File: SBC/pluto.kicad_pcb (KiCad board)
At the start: 4 copper layers, 114.3 x 120.9 mm, 60 parts, among them J1 VCC1, J10 GND3, J11 Expansion Bus, J2 GND1, J3 VCC2, J4 POWER, J5 GND2, J6 RS232a, J7 RS232b, J8 JTAG, J9 VCC3, P1 IDE0, SW1 RESET, U1 WD65C02PLCC44, U19 74LS574, U2 28C256, U20 74LS574, U21 74HC245, U22 MAX238, U23 SC28L92PLCC44, U3 AS6C62256A, U4 DS1511Y+, U5 TL7705B, U7 ispMACH4A5, U8 74HC74, X1 8 MHz, X2 3.6864MHz

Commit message: Preparation for Pluto v3.0
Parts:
- removed C21, C22: 0.1uF, Capacitors_ThroughHole:C_Disc_D4.7mm_W2.5mm_P5.00mm
- removed J8: JTAG, Connectors_IDC:IDC-Header_2x05_Pitch2.54mm_Straight
- removed MK2, MK5: Mounting_Hole, Mounting_Holes:MountingHole_3.2mm_M3_Pad
- removed R7: 1K, Resistors_ThroughHole:R_Axial_DIN0411_L9.9mm_D3.6mm_P12.70mm_Horizontal
- removed RN2: 3.3 kOhm, Resistors_THT:R_Array_SIP8
- removed U19, U20: 74LS574, Housings_DIP:DIP-20_W7.62mm_Socket
- removed U21: 74HC245, Housings_DIP:DIP-20_W7.62mm_Socket
- added C7: 0.1uF, Capacitor_THT:C_Disc_D4.7mm_W2.5mm_P5.00mm, F.Cu at (68.0, 97.2)
- added C8: 0.1uF, Capacitor_THT:C_Disc_D4.7mm_W2.5mm_P5.00mm, F.Cu at (86.3, 103.5)
- added C9: 0.1uF, Capacitor_THT:C_Disc_D4.7mm_W2.5mm_P5.00mm, F.Cu at (100.3, 82.5)
- added D2: DIRQ1, Diode_THT:D_T-1_P5.08mm_Horizontal, F.Cu at (86.4, 97.2)
- added D4: DIRQ2, Diode_THT:D_T-1_P5.08mm_Horizontal, F.Cu at (73.0, 103.5)
- added J12: VIA2PB, Connector_IDC:IDC-Header_2x07_P2.54mm_Vertical, F.Cu at (73.0, 136.5)
- added Q1: DS1813, Package_TO_SOT_THT:TO-92L_Inline, F.Cu at (125.7, 68.6)
- added SW2: PANIC, Button_Switch_THT:SW_PUSH_6mm_H4.3mm, F.Cu at (121.9, 62.9)
- added U6: PlutoDecoder, Package_DIP:DIP-24_W7.62mm_Socket, F.Cu at (95.2, 93.3)
- added U9: WD65C22PLCC44, Package_LCC:PLCC-44_THT-Socket, F.Cu at (71.8, 116.2)
- C1, C2, C20, C3, C5, C6: footprint Capacitors_ThroughHole:C_Disc_D4.7mm_W2.5mm_P5.00mm -> Capacitor_THT:C_Disc_D4.7mm_W2.5mm_P5.00mm
- C15, C16, C17, C18, C19, C4: footprint Capacitors_ThroughHole:CP_Radial_Tantal_D4.5mm_P2.50mm -> Capacitor_THT:CP_Radial_Tantal_D4.5mm_P2.50mm
- F1: footprint Fuse_Holders_and_Fuses:Fuseholder5x20_horiz_open_Schurter_0031_8201 -> Fuse:Fuseholder_Cylinder-5x20mm_Schurter_0031_8201_Horizontal_Open
- J1, J10, J2, J3, J5, J9: footprint Pin_Headers:Pin_Header_Straight_1x01_Pitch2.54mm -> Connector_PinHeader_2.54mm:PinHeader_1x01_P2.54mm_Vertical
- J11, P1: footprint Connectors_IDC:IDC-Header_2x20_Pitch2.54mm_Straight -> Connector_IDC:IDC-Header_2x20_P2.54mm_Vertical
- J4: footprint Connectors_Molex:Molex_NanoFit_1x04x2.50mm_Angled -> Connector_Molex:Molex_Nano-Fit_105313-xx04_1x04_P2.50mm_Horizontal
- J6, J7: footprint Connectors_IDC:IDC-Header_2x05_Pitch2.54mm_Straight -> Connector_IDC:IDC-Header_2x05_P2.54mm_Vertical
- MK1, MK3, MK4, MK6: footprint Mounting_Holes:MountingHole_3.2mm_M3_Pad -> MountingHole:MountingHole_3.2mm_M3_Pad
- R1, R6, R8: footprint Resistors_ThroughHole:R_Axial_DIN0411_L9.9mm_D3.6mm_P12.70mm_Horizontal -> Resistor_THT:R_Axial_DIN0411_L9.9mm_D3.6mm_P7.62mm_Vertical
- R2, R3, R4: footprint Resistors_ThroughHole:R_Axial_DIN0411_L9.9mm_D3.6mm_P7.62mm_Vertical -> Resistor_THT:R_Axial_DIN0411_L9.9mm_D3.6mm_P7.62mm_Vertical
- RN1: value 3.3 kOhm -> 3.3k; footprint Resistors_THT:R_Array_SIP8 -> Resistor_THT:R_Array_SIP9
- SW1: footprint Buttons_Switches_ThroughHole:SW_PUSH_6mm_h4.3mm -> Button_Switch_THT:SW_PUSH_6mm_H4.3mm
- U1, U23: footprint Housings_LCC:PLCC-44_THT-Socket -> Package_LCC:PLCC-44_THT-Socket
- U2: value 28C256 -> AT28HC256EPLCC32; footprint Housings_DIP:DIP-28_W15.24mm_Socket -> Grotto:PLCC-32_THT-Socket
- U22: footprint Housings_DIP:DIP-24_W7.62mm_Socket -> Package_DIP:DIP-24_W7.62mm_Socket
- U3: footprint Housings_DIP:DIP-28_W15.24mm_Socket -> Package_DIP:DIP-28_W7.62mm_Socket
- U4: footprint Housings_DIP:DIP-28_W15.24mm_Socket -> Package_DIP:DIP-28_W15.24mm_Socket
- U5: footprint Housings_DIP:DIP-8_W7.62mm_Socket -> Package_DIP:DIP-8_W7.62mm_Socket
- U7: value ispMACH4A5 -> WD65C22PLCC44; footprint Housings_LCC:PLCC-44_THT-Socket -> Package_LCC:PLCC-44_THT-Socket
- U8: footprint Housings_DIP:DIP-14_W7.62mm_Socket -> Package_DIP:DIP-14_W7.62mm_Socket
- X1, X2: footprint Oscillators:Oscillator_DIP-8 -> Oscillator:Oscillator_DIP-8
- moved J2 94.1 mm to (158.2, 59.1), turned to 90 degrees
- moved C2 86.4 mm to (150.5, 72.4), turned to 0 degrees
- moved J1 85.4 mm to (158.2, 62.9), turned to 90 degrees
- moved R3 78.1 mm to (139.7, 59.7), turned to 180 degrees
- moved R2 76.3 mm to (154.3, 47.0), turned to 270 degrees
- moved C4 72.6 mm to (132.1, 55.9), turned to 90 degrees
- moved R4 68.7 mm to (137.8, 54.0), turned to 90 degrees
- moved U3 62.3 mm to (149.2, 75.6), turned to 0 degrees
- moved U2 60.8 mm to (136.5, 90.8), turned to 0 degrees
- moved J11 60.0 mm to (104.8, 136.1), turned to 90 degrees
- moved C3 53.9 mm to (139.7, 78.1), turned to 180 degrees
- moved U8 51.3 mm to (95.2, 62.2), turned to 0 degrees
- moved RN1 46.7 mm to (115.6, 99.1), turned to 180 degrees
- moved U1 39.1 mm to (108.0, 123.8), turned to 180 degrees
- moved J3 36.6 mm to (130.7, 49.4), turned to 270 degrees
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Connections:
- net /16bit IDE interface/~IDE:DASP renamed /16bit IDE interface/~IDE-DASP
- net /16bit IDE interface/~IDE:DMACK renamed /16bit IDE interface/~IDE-DMACK
- J11 pad 24: /Address decoding and support section/R/~W -> /16bit IDE interface/R-~W
- J11 pad 34: /Address decoding and support section/~7FCX -> /Address decoding and support section/~IO
- J11 pad 36: /Address decoding and support section/~7FAX -> Net-(J11-Pad36)
- J11 pad 38: /Address decoding and support section/CLK -> /16bit IDE interface/CLK
- J11 pad 9: /Address decoding and support section/A3 -> /16bit IDE interface/A3
- P1 pad 1: /16bit IDE interface/~RES -> /16bit IDE interface/~IDE-RES
- P1 pad 23: /16bit IDE interface/DIOW -> /16bit IDE interface/~DIOW
- P1 pad 25: /16bit IDE interface/DIOR -> /16bit IDE interface/~DIOR
- P1 pad 33: /16bit IDE interface/A1 -> /16bit IDE interface/IDE-A1
- P1 pad 35: /16bit IDE interface/A0 -> /16bit IDE interface/IDE-A0
- P1 pad 36: /16bit IDE interface/A2 -> /16bit IDE interface/IDE-A2
- P1 pad 37: /16bit IDE interface/IDE_CS0 -> /16bit IDE interface/~IDE-CS0
- P1 pad 38: /16bit IDE interface/~IDE:CS1 -> /16bit IDE interface/~IDE-CS1
- R2 pad 1: Net-(R2-Pad1) -> VCC
- R2 pad 2: VCC -> Net-(R2-Pad2)
- RN1 pad 2: Net-(RN1-Pad2) -> /16bit IDE interface/~RES
- RN1 pad 4: /Address decoding and support section/TDO -> /Address decoding and support section/~SO
- RN1 pad 5: /Address decoding and support section/TDI -> /Address decoding and support section/RDY
- RN1 pad 6: /Address decoding and support section/TMS -> /Address decoding and support section/~PWR
- RN1 pad 7: /Address decoding and support section/TCK -> /Address decoding and support section/BE
- RN1 pad 8: /Address decoding and support section/~SO -> /Address decoding and support section/~NMI
- SW1 pad 2: Net-(R2-Pad1) -> Net-(R2-Pad2)
- U1 pad 14: /Address decoding and support section/A3 -> /16bit IDE interface/A3
- U1 pad 38: /Address decoding and support section/R/~W -> /16bit IDE interface/R-~W
- U1 pad 41: /Address decoding and support section/CLK -> /16bit IDE interface/CLK
- U2 pad 1: /Address decoding and support section/A14 -> Net-(U2-Pad1)
- U2 pad 10: /16bit IDE interface/A0 -> /16bit IDE interface/A1
- U2 pad 11: /16bit IDE interface/D0 -> /16bit IDE interface/A0
- U2 pad 12: /16bit IDE interface/D1 -> Net-(U2-Pad12)
- U2 pad 13: /16bit IDE interface/D2 -> /16bit IDE interface/D0
- U2 pad 14: GND -> /16bit IDE interface/D1
- U2 pad 15: /16bit IDE interface/D3 -> /16bit IDE interface/D2
- U2 pad 16: /16bit IDE interface/D4 -> GND
- U2 pad 17: /16bit IDE interface/D5 -> Net-(U2-Pad17)
- U2 pad 18: /16bit IDE interface/D6 -> /16bit IDE interface/D3
- U2 pad 19: /16bit IDE interface/D7 -> /16bit IDE interface/D4
- U2 pad 2: /Address decoding and support section/A12 -> /Address decoding and support section/A14
- U2 pad 20: /Address decoding and support section/~ROMSEL -> /16bit IDE interface/D5
- U2 pad 21: /Address decoding and support section/A10 -> /16bit IDE interface/D6
- U2 pad 22: /Address decoding and support section/~MRD -> /16bit IDE interface/D7
- U2 pad 23: /Address decoding and support section/A11 -> /Address decoding and support section/~ROMSEL
- U2 pad 24: /Address decoding and support section/A9 -> /Address decoding and support section/A10
- U2 pad 25: /Address decoding and support section/A8 -> /Address decoding and support section/~MRD
- U2 pad 26: /Address decoding and support section/A13 -> Net-(U2-Pad26)
- U2 pad 27: VCC -> /Address decoding and support section/A11
- U2 pad 28: VCC -> /Address decoding and support section/A9
- U2 pad 3: /Address decoding and support section/A7 -> /Address decoding and support section/A12
- U2 pad 4: /Address decoding and support section/A6 -> /Address decoding and support section/A7
- U2 pad 5: /Address decoding and support section/A5 -> /Address decoding and support section/A6
- U2 pad 6: /CPU, ROM and RAM/A4 -> /Address decoding and support section/A5
- U2 pad 7: /Address decoding and support section/A3 -> /CPU, ROM and RAM/A4
- U2 pad 8: /16bit IDE interface/A2 -> /16bit IDE interface/A3
- U2 pad 9: /16bit IDE interface/A1 -> /16bit IDE interface/A2
- U23 pad 39: /Address decoding and support section/~7FEX -> /Address decoding and support section/~DUART
- U23 pad 7: /Address decoding and support section/A3 -> /16bit IDE interface/A3
- U3 pad 7: /Address decoding and support section/A3 -> /16bit IDE interface/A3
- U4 pad 20: /Address decoding and support section/~7F8X -> /Address decoding and support section/~RTC
- U4 pad 7: /Address decoding and support section/A3 -> /16bit IDE interface/A3
- U5 pad 2: Net-(R2-Pad1) -> Net-(R2-Pad2)
- U7 pad 10: /Address decoding and support section/TDI -> /16bit IDE interface/IDE-D8
- U7 pad 11: /Address decoding and support section/CLK -> Net-(U7-Pad11)
- U7 pad 12: GND -> /16bit IDE interface/IDE-D9
- U7 pad 13: /Address decoding and support section/TCK -> /16bit IDE interface/IDE-D10
- U7 pad 14: /Address decoding and support section/A13 -> /16bit IDE interface/IDE-D11
- U7 pad 15: /Address decoding and support section/~RAMSEL -> /16bit IDE interface/IDE-D12
- U7 pad 16: /Address decoding and support section/A12 -> /16bit IDE interface/IDE-D13
- U7 pad 17: /16bit IDE interface/FROM_CLK -> /16bit IDE interface/IDE-D14
- U7 pad 18: /Address decoding and support section/A11 -> /16bit IDE interface/IDE-D15
- U7 pad 19: /16bit IDE interface/IDE_CS0 -> Net-(U7-Pad19)
- U7 pad 2: /Address decoding and support section/~7FAX -> /16bit IDE interface/IDE-D0
- U7 pad 20: /16bit IDE interface/OBT_OE -> Net-(U7-Pad20)
- U7 pad 21: /Address decoding and support section/~ROMSEL -> VCC
- U7 pad 22: VCC -> Net-(U7-Pad22)
- U7 pad 23: GND -> Net-(D2-Pad1)
- U7 pad 24: /16bit IDE interface/FROM_OE -> /16bit IDE interface/R-~W
- U7 pad 25: /16bit IDE interface/DIOW -> /16bit IDE interface/~VIA1SEL
- U7 pad 26: /16bit IDE interface/TO_OE -> VCC
- U7 pad 27: /Address decoding and support section/A10 -> /16bit IDE interface/CLK
- U7 pad 28: /16bit IDE interface/OBT_DIR -> /16bit IDE interface/D7
- U7 pad 29: /Address decoding and support section/A9 -> /16bit IDE interface/D6
- U7 pad 3: /Address decoding and support section/~7FEX -> /16bit IDE interface/IDE-D1
- U7 pad 30: /16bit IDE interface/TO_CLK -> /16bit IDE interface/D5
- U7 pad 31: /Address decoding and support section/A8 -> /16bit IDE interface/D4
- U7 pad 32: /Address decoding and support section/TMS -> /16bit IDE interface/D3
- U7 pad 33: /Address decoding and support section/A15 -> Net-(U7-Pad33)
- U7 pad 34: GND -> /16bit IDE interface/D2
- U7 pad 35: /Address decoding and support section/TDO -> /16bit IDE interface/D1
- U7 pad 36: /Address decoding and support section/A7 -> /16bit IDE interface/D0
- U7 pad 37: Net-(U7-Pad37) -> /16bit IDE interface/~RES
- U7 pad 38: /Address decoding and support section/A6 -> Net-(U7-Pad38)
- U7 pad 39: /16bit IDE interface/DIOR -> /16bit IDE interface/A3
- U7 pad 4: Net-(U7-Pad4) -> /16bit IDE interface/IDE-D2
- U7 pad 40: /Address decoding and support section/A5 -> /16bit IDE interface/A2
- U7 pad 41: /Address decoding and support section/~MRD -> /16bit IDE interface/A1
- U7 pad 42: Net-(U7-Pad42) -> /16bit IDE interface/A0
- U7 pad 43: /Address decoding and support section/~MWR -> Net-(U7-Pad43)
- U7 pad 44: VCC -> Net-(U7-Pad44)
- U7 pad 5: /Address decoding and support section/A3 -> /16bit IDE interface/IDE-D3
- U7 pad 6: /Address decoding and support section/~7F8X -> /16bit IDE interface/IDE-D4
- U7 pad 7: /Address decoding and support section/R/~W -> /16bit IDE interface/IDE-D5
- U7 pad 8: /Address decoding and support section/~7FCX -> /16bit IDE interface/IDE-D6
- U7 pad 9: /Address decoding and support section/A14 -> /16bit IDE interface/IDE-D7
- U8 pad 9: /Address decoding and support section/CLK -> /16bit IDE interface/CLK
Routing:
- net /16bit IDE interface/D6: track 260.5 -> 0.00 mm
- net /16bit IDE interface/D7: track 256.1 -> 0.00 mm, vias 1 -> 0
- net /16bit IDE interface/D5: track 223.3 -> 0.00 mm, vias 1 -> 0
- net /16bit IDE interface/D4: track 217.7 -> 0.00 mm, vias 2 -> 0
- net /16bit IDE interface/~IRQ: track 211.2 -> 0.00 mm, vias 1 -> 0
- net /16bit IDE interface/D3: track 205.0 -> 0.00 mm, vias 2 -> 0
- net /16bit IDE interface/A0: track 196.0 -> 0.00 mm
- net /16bit IDE interface/D0: track 194.8 -> 0.00 mm
- net /16bit IDE interface/D2: track 191.6 -> 0.00 mm, vias 1 -> 0
- net /16bit IDE interface/A1: track 189.8 -> 0.00 mm
- net /16bit IDE interface/~RES: track 186.1 -> 0.00 mm, vias 2 -> 0
- net /Address decoding and support section/~MRD: track 185.4 -> 0.00 mm, vias 1 -> 0
- net /16bit IDE interface/A2: track 185.3 -> 0.00 mm
- net /16bit IDE interface/D1: track 181.6 -> 0.00 mm, vias 2 -> 0
- net /Address decoding and support section/~MWR: track 179.2 -> 0.00 mm
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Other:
- board text added: "Pluto V3.0 Jul 2019 © Johan Groth"
- board text removed: "Pluto V2.0 Dec 2017 © Johan Groth"

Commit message: A better layout of PCB.
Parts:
- moved J9 72.9 mm to (158.1, 48.9), turned to 90 degrees
- moved J10 68.8 mm to (147.3, 48.9), turned to 90 degrees
- moved J3 28.2 mm to (158.1, 55.9), turned to 90 degrees
- moved R3 24.2 mm to (115.6, 61.6)
- moved Q1 22.9 mm to (106.7, 81.3)
- moved J5 21.8 mm to (147.3, 55.9), turned to 90 degrees
- moved C3 21.0 mm to (160.7, 80.0), turned to 90 degrees
- moved C2 20.5 mm to (132.7, 82.5)
- moved R2 18.1 mm to (136.5, 50.2), turned to 180 degrees
- moved R4 16.9 mm to (123.8, 63.5)
- moved U5 16.8 mm to (136.5, 64.1)
- moved C4 16.5 mm to (115.6, 56.5), turned to 0 degrees
- moved SW2 16.3 mm to (132.1, 75.6), turned to 180 degrees
- moved J2 11.6 mm to (147.3, 62.9)
- moved C6 10.9 mm to (140.3, 61.6), turned to 90 degrees
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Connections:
- U6 pad 14: /16bit IDE interface/~VIA2SEL -> /Address decoding and support section/~IO
- U6 pad 15: /Address decoding and support section/~DUART -> /Address decoding and support section/~RTC
- U6 pad 16: /Address decoding and support section/~RAMSEL -> /16bit IDE interface/~VIA2SEL
- U6 pad 17: /Address decoding and support section/~MRD -> /Address decoding and support section/~DUART
- U6 pad 18: /Address decoding and support section/~IO -> /Address decoding and support section/~RAMSEL
- U6 pad 19: /16bit IDE interface/R-~W -> /Address decoding and support section/~ROMSEL
- U6 pad 20: /Address decoding and support section/~MWR -> /16bit IDE interface/~VIA1SEL
- U6 pad 21: /Address decoding and support section/~ROMSEL -> /Address decoding and support section/~MWR
- U6 pad 22: /16bit IDE interface/~VIA1SEL -> /Address decoding and support section/~MRD
- U6 pad 23: /Address decoding and support section/~RTC -> /16bit IDE interface/R-~W

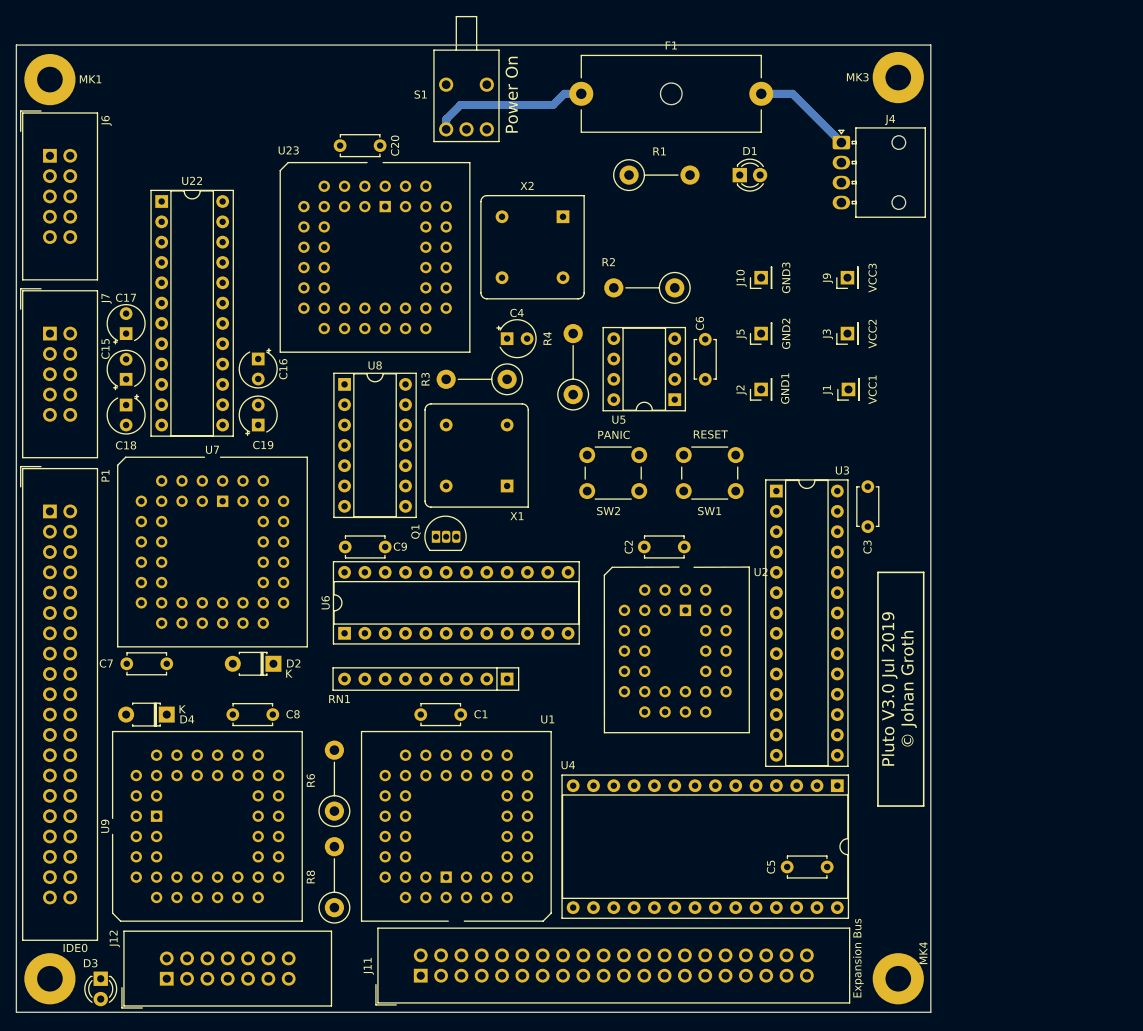
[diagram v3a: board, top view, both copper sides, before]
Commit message: Autorouting of Pluto v3.0 complete. Fixed VCC/GND and IDE-A2(!)
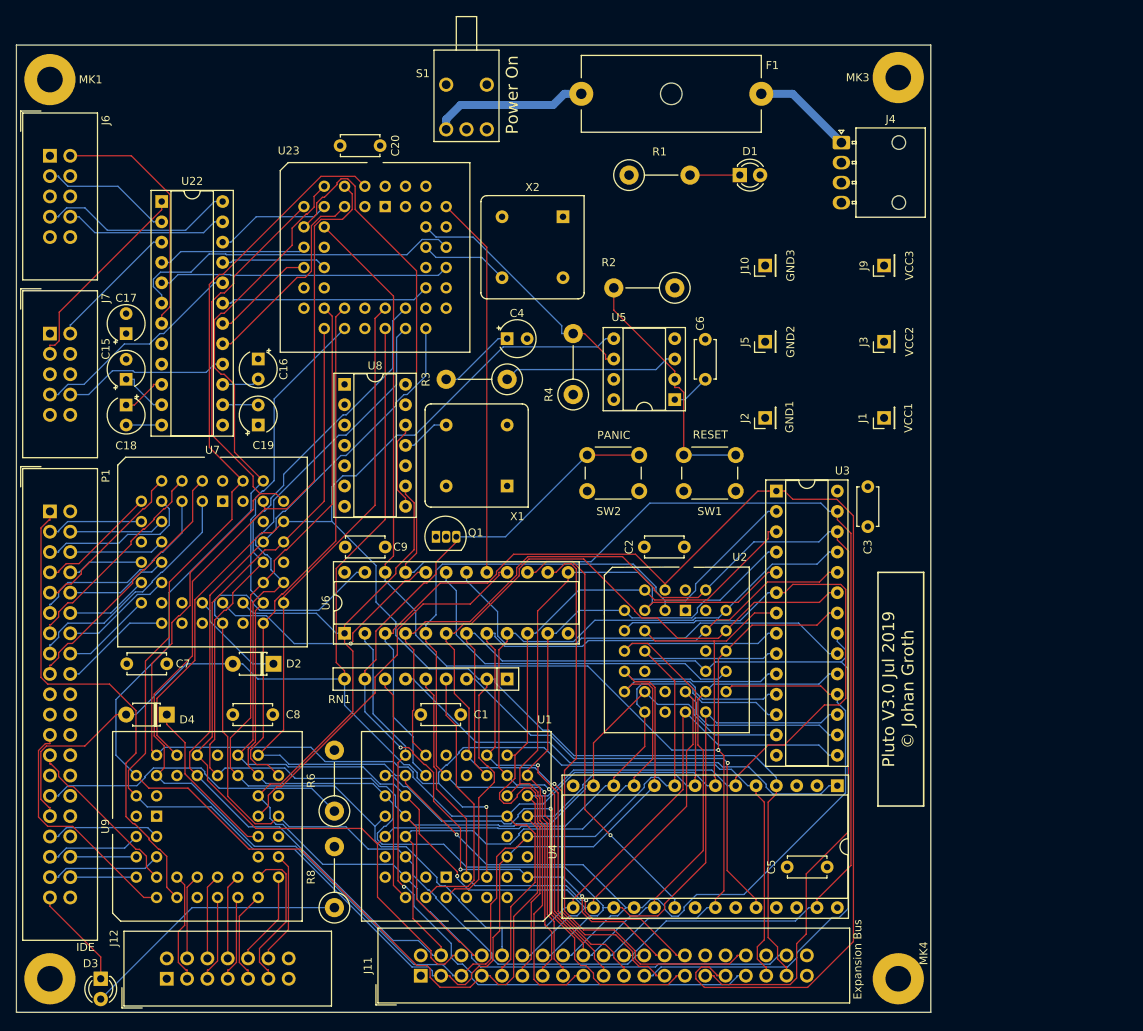
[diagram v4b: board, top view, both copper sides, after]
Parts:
- P1: value IDE0 -> IDE
- moved J1 5.69 mm to (162.7, 66.4)
- moved J9 4.82 mm to (162.7, 47.4)
- moved J3 4.68 mm to (162.7, 56.9)
- moved J2 3.59 mm to (147.8, 66.4)
- moved J10 1.61 mm to (147.8, 47.4)
- moved J5 1.14 mm to (147.8, 56.9)
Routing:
- net /16bit IDE interface/A2: track 0.00 -> 240.6 mm
- net /16bit IDE interface/A0: track 0.00 -> 226.6 mm
- net /16bit IDE interface/A3: track 0.00 -> 223.1 mm
- net /16bit IDE interface/~RES: track 0.00 -> 222.0 mm
- net /16bit IDE interface/A1: track 0.00 -> 218.1 mm
- net /16bit IDE interface/~IRQ: track 0.00 -> 203.6 mm, vias 0 -> 1
- net /Address decoding and support section/~MWR: track 0.00 -> 198.9 mm
- net /16bit IDE interface/D0: track 0.00 -> 196.8 mm
- net /16bit IDE interface/D6: track 0.00 -> 190.3 mm, vias 0 -> 1
- net /16bit IDE interface/D4: track 0.00 -> 186.0 mm, vias 0 -> 1
- net /16bit IDE interface/D7: track 0.00 -> 182.1 mm, vias 0 -> 1
- net /16bit IDE interface/D5: track 0.00 -> 181.3 mm
- net /16bit IDE interface/D2: track 0.00 -> 179.5 mm
- net /16bit IDE interface/D1: track 0.00 -> 176.9 mm
- net /16bit IDE interface/D3: track 0.00 -> 173.7 mm
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
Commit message: Converting to SMD of almost all components.
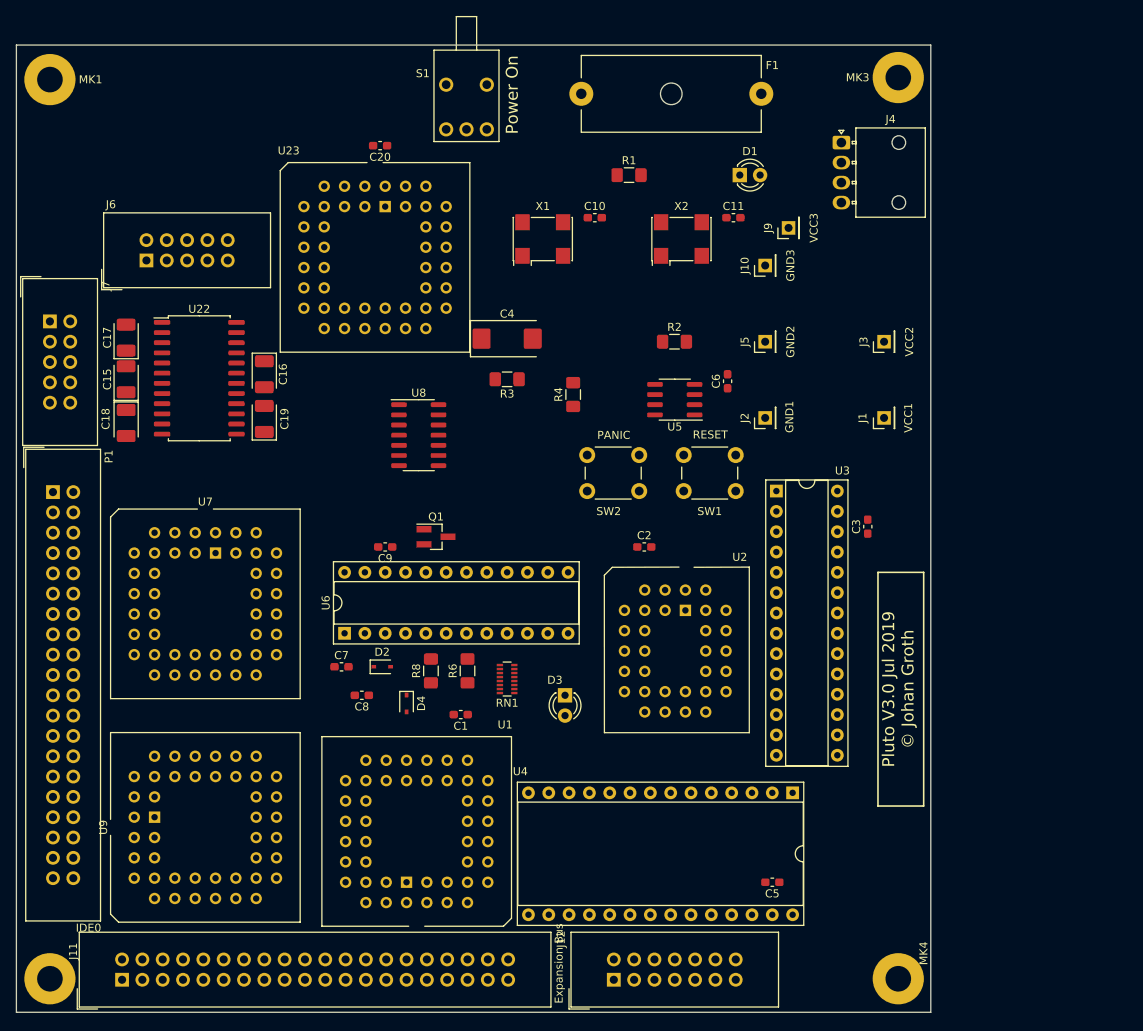
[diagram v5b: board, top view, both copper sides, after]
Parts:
- added C10: 0.1uF, Capacitor_SMD:C_0603_1608Metric_Pad1.05x0.95mm_HandSolder, F.Cu at (126.5, 41.4)
- added C11: 0.1uF, Capacitor_SMD:C_0603_1608Metric_Pad1.05x0.95mm_HandSolder, F.Cu at (143.9, 41.4)
- C1, C2, C20, C3, C5, C6, C7, C8, C9: footprint Capacitor_THT:C_Disc_D4.7mm_W2.5mm_P5.00mm -> Capacitor_SMD:C_0603_1608Metric_Pad1.05x0.95mm_HandSolder
- C15, C16, C17, C18, C19: footprint Capacitor_THT:CP_Radial_Tantal_D4.5mm_P2.50mm -> Capacitor_Tantalum_SMD:CP_EIA-3528-21_Kemet-B_Pad1.50x2.35mm_HandSolder
- C4: footprint Capacitor_THT:CP_Radial_Tantal_D4.5mm_P2.50mm -> Capacitor_Tantalum_SMD:CP_EIA-7343-31_Kemet-D_Pad2.25x2.55mm_HandSolder
- D2, D4: footprint Diode_THT:D_T-1_P5.08mm_Horizontal -> Diode_SMD:D_SOD-323
- P1: value IDE -> IDE0
- Q1: footprint Package_TO_SOT_THT:TO-92L_Inline -> Package_TO_SOT_SMD:SOT-23_Handsoldering
- R1, R2, R3, R4, R6, R8: footprint Resistor_THT:R_Axial_DIN0411_L9.9mm_D3.6mm_P7.62mm_Vertical -> Resistor_SMD:R_1206_3216Metric_Pad1.42x1.75mm_HandSolder
- RN1: footprint Resistor_THT:R_Array_SIP9 -> Resistor_SMD:R_Array_Convex_8x0602
- U22: footprint Package_DIP:DIP-24_W7.62mm_Socket -> Package_SO:SOIC-24W_7.5x15.4mm_P1.27mm
- U5: footprint Package_DIP:DIP-8_W7.62mm_Socket -> Package_SO:SOIC-8_3.9x4.9mm_P1.27mm
- U8: footprint Package_DIP:DIP-14_W7.62mm_Socket -> Package_SO:SOIC-14_3.9x8.7mm_P1.27mm
- X1: value 8 MHz -> 8MHz; footprint Oscillator:Oscillator_DIP-8 -> Oscillator:Oscillator_SMD_SeikoEpson_SG8002CA-4Pin_7.0x5.0mm
- X2: footprint Oscillator:Oscillator_DIP-8 -> Oscillator:Oscillator_SMD_SeikoEpson_SG8002CA-4Pin_7.0x5.0mm
- moved D3 68.0 mm to (122.8, 101.1)
- moved J12 55.9 mm to (128.9, 136.7)
- moved J11 37.3 mm to (67.4, 136.7)
- moved R8 32.0 mm to (106.0, 98.0)
- moved X1 31.2 mm to (120.0, 44.1), turned to 0 degrees
- moved D4 30.0 mm to (103.0, 102.1), turned to 270 degrees
- moved C7 26.8 mm to (94.9, 97.5)
- moved R6 24.2 mm to (110.6, 98.0)
- moved U22 22.6 mm to (77.1, 61.5)
- moved J6 17.8 mm to (70.5, 46.7), turned to 90 degrees
- moved X2 15.1 mm to (137.4, 44.1), turned to 0 degrees
- moved D2 13.6 mm to (99.9, 97.5), turned to 0 degrees
- moved J9 12.8 mm to (150.7, 42.7)
- moved C8 11.4 mm to (97.4, 101.1)
- moved U8 11.2 mm to (104.5, 68.6)
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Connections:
- X1 pad 1: Net-(X1-Pad1) -> VCC
- X1 pad 4: GND -> VCC
- X2 pad 1: Net-(X2-Pad1) -> VCC
- X2 pad 4: GND -> VCC
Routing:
- net /16bit IDE interface/A2: track 240.6 -> 0.00 mm
- net /16bit IDE interface/A0: track 226.6 -> 0.00 mm
- net /16bit IDE interface/A3: track 223.1 -> 0.00 mm
- net /16bit IDE interface/~RES: track 222.0 -> 0.00 mm
- net /16bit IDE interface/A1: track 218.1 -> 0.00 mm
- net /16bit IDE interface/~IRQ: track 203.6 -> 0.00 mm, vias 1 -> 0
- net /Address decoding and support section/~MWR: track 198.9 -> 0.00 mm
- net /16bit IDE interface/D0: track 196.8 -> 0.00 mm
- net /16bit IDE interface/D6: track 190.3 -> 0.00 mm, vias 1 -> 0
- net /16bit IDE interface/D4: track 186.0 -> 0.00 mm, vias 1 -> 0
- net /16bit IDE interface/D7: track 182.1 -> 0.00 mm, vias 1 -> 0
- net /16bit IDE interface/D5: track 181.3 -> 0.00 mm
- net /16bit IDE interface/D2: track 179.5 -> 0.00 mm
- net /16bit IDE interface/D1: track 176.9 -> 0.00 mm
- net /16bit IDE interface/D3: track 173.7 -> 0.00 mm
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
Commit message: New PCB layout is taking shape.
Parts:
- C1, C10, C11, C2, C20, C3, C5, C6, C7, C8, C9: footprint Capacitor_SMD:C_0603_1608Metric_Pad1.05x0.95mm_HandSolder -> Capacitor_SMD:C_0805_2012Metric_Pad1.15x1.40mm_HandSolder
- RN1: footprint Resistor_SMD:R_Array_Convex_8x0602 -> Resistor_SMD:R_Array_Convex_5x1206
- U3: value AS6C62256A -> IS61C256AL-12JLI; footprint Package_DIP:DIP-28_W7.62mm_Socket -> Package_SO:SOJ-28_7.585x18.12mm_P1.27mm
- moved C6 61.3 mm to (81.9, 57.8)
- moved R6 61.1 mm to (59.0, 130.7), turned to 180 degrees
- moved R2 56.3 mm to (80.4, 51.6), turned to 90 degrees
- moved U5 50.4 mm to (86.7, 56.9)
- moved C11 43.8 mm to (126.2, 81.4), turned to 270 degrees
- moved J10 42.5 mm to (188.8, 58.5)
- moved J2 42.5 mm to (188.8, 77.5)
- moved J5 42.5 mm to (188.8, 68.0)
- moved SW1 40.6 mm to (106.6, 60.2)
- moved X2 38.8 mm to (121.6, 79.5), turned to 90 degrees
- moved R4 37.4 mm to (88.0, 52.7), turned to 180 degrees
- moved C10 33.3 mm to (120.0, 74.0), turned to 180 degrees
- moved C20 33.0 mm to (106.2, 64.8)
- moved U23 32.5 mm to (106.9, 71.8)
- moved C3 28.4 mm to (146.2, 104.4), turned to 0 degrees
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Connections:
- RN1 pad 1: VCC -> /16bit IDE interface/~RES
- RN1 pad 10: (no net) -> VCC
- RN1 pad 2: /16bit IDE interface/~RES -> /Address decoding and support section/~KS
- RN1 pad 3: /Address decoding and support section/~KS -> /Address decoding and support section/~SO
- RN1 pad 4: /Address decoding and support section/~SO -> /Address decoding and support section/RDY
- RN1 pad 5: /Address decoding and support section/RDY -> VCC

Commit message: Added datasheets for 7-seg LED Kingbright displays.
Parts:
- moved J2 115.9 mm to (72.9, 75.4)
- moved J1 114.1 mm to (67.4, 75.4)
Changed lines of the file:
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@@
   )
   (module Connector_PinHeader_2.54mm:PinHeader_1x01_P2.54mm_Vertical (layer F.Cu)
-    (at 180.8734 63.5 90)
+    (at 67.437 75.3872 90)
     (descr "Through hole straight pin header, 1x01, 2.54mm pitch, single row")
     (tags "Through hole pin header THT 1x01 2.54mm single row")
-    (fp_text reference J1 (at 0 -2.667 90) (layer F.SilkS)
+    (fp_text reference J1 (at 2.4892 -1.2192 180) (layer F.SilkS)
       (effects (font (size 1 1) (thickness 0.15)))
     )
-    (fp_text value VCC1 (at 0 3.048 90) (layer F.SilkS)
+    (fp_text value VCC1 (at 2.4892 1.4732 180) (layer F.SilkS)
       (effects (font (size 1 1) (thickness 0.15)))
     )
@@
   )
   (module Connector_PinHeader_2.54mm:PinHeader_1x01_P2.54mm_Vertical (layer F.Cu)
-    (at 188.8236 77.5462 90)
+    (at 72.9234 75.3872 90)
     (descr "Through hole straight pin header, 1x01, 2.54mm pitch, single row")
     (tags "Through hole pin header THT 1x01 2.54mm single row")
-    (fp_text reference J2 (at 0 -2.54 90) (layer F.SilkS)
+    (fp_text reference J2 (at -0.9652 -2.54 270) (layer F.SilkS)
       (effects (font (size 1 1) (thickness 0.15)))
     )
-    (fp_text value GND1 (at 0.127 3.048 90) (layer F.SilkS)
+    (fp_text value GND1 (at 2.54 -0.2032 180) (layer F.SilkS)
       (effects (font (size 1 1) (thickness 0.15)))
     )
